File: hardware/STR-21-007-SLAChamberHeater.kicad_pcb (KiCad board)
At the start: 0 parts

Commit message: schematics finished, footprints assigned. Still need to fix foorptints for MOSFETS
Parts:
- added C101: 10n, Capacitor_SMD:C_0603_1608Metric, F.Cu at (88.9, 127.0)
- added C102: 10u, Capacitor_SMD:C_1206_3216Metric, F.Cu at (71.5, 132.3)
- added C103: 10u, Capacitor_SMD:C_1206_3216Metric, F.Cu at (90.3, 119.0)
- added C104: 10u, Capacitor_SMD:C_1206_3216Metric, F.Cu at (84.6, 122.3)
- added C201: 1u, Capacitor_SMD:C_0402_1005Metric, F.Cu at (75.3, 156.5)
- added C202: 10u, Capacitor_SMD:C_0402_1005Metric, F.Cu at (75.3, 158.5)
- added C203: 100n, Capacitor_SMD:C_0402_1005Metric, F.Cu at (79.7, 155.4)
- added C204: 100n, Capacitor_SMD:C_0402_1005Metric, F.Cu at (91.3, 143.4)
- added C301: 1u, Capacitor_SMD:C_0402_1005Metric, F.Cu at (136.1, 122.0)
- added C302: 100n, Capacitor_SMD:C_0402_1005Metric, F.Cu at (129.4, 127.6)
- added C303: 1u, Capacitor_SMD:C_0402_1005Metric, F.Cu at (132.3, 127.6)
- added C304: 100n, Capacitor_SMD:C_0402_1005Metric, F.Cu at (132.3, 125.6)
- added D101: B5819W, Diode_SMD:D_SOD-123, F.Cu at (92.2, 112.2)
- added D102: B5819W, Diode_SMD:D_SOD-123, F.Cu at (84.6, 119.0)
- added D103: B5819W, Diode_SMD:D_SOD-123, F.Cu at (65.8, 132.3)
- added D301: 1N4148W, Diode_SMD:D_SOD-123, F.Cu at (131.4, 112.2)
- added F101: 5A, Fuse:Fuse_1206_3216Metric, F.Cu at (92.1, 115.5)
- added FB101: 600@600MHz, Inductor_SMD:L_0805_2012Metric, F.Cu at (76.6, 132.0)
- added H1: MountingHole, MountingHole:MountingHole_2.2mm_M2, F.Cu at (113.5, 140.4)
- added H2: MountingHole, MountingHole:MountingHole_2.2mm_M2, F.Cu at (107.5, 146.3)
- added H3: MountingHole, MountingHole:MountingHole_2.2mm_M2, F.Cu at (107.5, 140.4)
- added H4: MountingHole, MountingHole:MountingHole_2.2mm_M2, F.Cu at (113.5, 146.3)
- added J101: 2.5mm, Connector_BarrelJack:BarrelJack_CUI_PJ-036AH-SMT_Horizontal, F.Cu at (72.3, 119.6)
- added J201: USB_C_Receptacle_USB2.0, STR-USB:USB_C_Receptacle_C136423, F.Cu at (44.5, 152.4)
- added J301: HEATER, TerminalBlock_Phoenix:TerminalBlock_Phoenix_PT-1,5-2-3.5-H_1x02_P3.50mm_Horizontal, F.Cu at (165.1, 127.0)
- added J302: FAN, Connector_JST:JST_EH_B2B-EH-A_1x02_P2.50mm_Vertical, F.Cu at (165.1, 139.7)
- added J401: OLED, Connector_PinHeader_2.54mm:PinHeader_1x04_P2.54mm_Vertical_SMD_Pin1Left, F.Cu at (134.4, 138.7)
- added L101: 10u, Inductor_SMD:L_Sunlord_MWSA0518_5.4x5.2mm, F.Cu at (85.5, 113.9)
- added LED101: Green, LED_SMD:LED_0603_1608Metric, F.Cu at (89.4, 121.9)
- added LED301: Blue, LED_SMD:LED_0603_1608Metric, F.Cu at (135.9, 117.8)
- added LED302: Red, LED_SMD:LED_0603_1608Metric, F.Cu at (135.9, 115.2)
- added LED401: WS2812B, STR-LED:WS2812B, F.Cu at (142.2, 154.1)
- added Q101: RU30L30M3, Package_DFN_QFN:DFN-8-1EP_3x3mm_P0.65mm_EP1.7x2.05mm, F.Cu at (152.4, 108.0)
- added Q301: BSS138, Package_TO_SOT_SMD:SOT-23, F.Cu at (129.3, 122.4)
- added Q302: RU30L30M3, Package_DFN_QFN:DFN-8-1EP_3x3mm_P0.65mm_EP1.7x2.05mm, F.Cu at (152.4, 120.7)
- added Q303: RU3070M3, STR-DFN:DFN-8-1EP_3x3mm_P0.65mm_EP1.7x2.05mm, F.Cu at (152.4, 114.3)
- added Q304: BSS138, Package_TO_SOT_SMD:SOT-23, F.Cu at (125.5, 127.0)
- added R101: 100K, Resistor_SMD:R_0603_1608Metric, F.Cu at (99.2, 116.3)
- added R102: 68K, Resistor_SMD:R_0603_1608Metric, F.Cu at (102.3, 111.8)
- added R103: 47K, Resistor_SMD:R_0603_1608Metric, F.Cu at (80.8, 131.8)
- added R104: 15K, Resistor_SMD:R_0603_1608Metric, F.Cu at (95.2, 118.4)
- added R105: 270, Resistor_SMD:R_0603_1608Metric, F.Cu at (93.5, 121.9)
- added R106: 1K5, Resistor_SMD:R_0603_1608Metric, F.Cu at (89.4, 124.5)
- added R201: 10K, Resistor_SMD:R_0402_1005Metric, F.Cu at (72.4, 156.5)
- added R202: 10K, Resistor_SMD:R_0402_1005Metric, F.Cu at (79.7, 153.4)
- added R203: 2k2, Resistor_SMD:R_0402_1005Metric, F.Cu at (69.5, 158.5)
- added R204: 2k2, Resistor_SMD:R_0402_1005Metric, F.Cu at (69.5, 156.5)
- added R205: 10K, Resistor_SMD:R_0402_1005Metric, F.Cu at (72.4, 158.5)
- added R207: 5K1, Resistor_SMD:R_0402_1005Metric, F.Cu at (82.6, 153.4)
- added R208: 5K1, Resistor_SMD:R_0402_1005Metric, F.Cu at (89.9, 148.4)
- added R301: 100R, Resistor_SMD:R_0402_1005Metric, F.Cu at (109.7, 128.1)
- added R302: 100R, Resistor_SMD:R_0402_1005Metric, F.Cu at (115.6, 128.1)
- added R303: 10K, Resistor_SMD:R_0402_1005Metric, F.Cu at (129.4, 125.6)
- added R304: 10K, Resistor_SMD:R_0402_1005Metric, F.Cu at (133.2, 120.1)
- added R305: 100R, Resistor_SMD:R_0402_1005Metric, F.Cu at (136.1, 120.1)
- added R306: 10K, Resistor_SMD:R_0402_1005Metric, F.Cu at (133.2, 122.1)
- added R307: 1K5, Resistor_SMD:R_0402_1005Metric, F.Cu at (112.7, 128.1)
- added R308: 1K5, Resistor_SMD:R_0402_1005Metric, F.Cu at (135.8, 111.5)
- added SW201: SW_Push, STR-Switch:SW_SMD_SPST_8x3.6, F.Cu at (101.6, 177.8)
- added SW202: SW_Push, STR-Switch:SW_SMD_SPST_8x3.6, F.Cu at (101.6, 165.1)
- added SW401: SW_Push, STR-Switch:SW_SMD_SPST_8x3.6, F.Cu at (127.0, 165.1)
- added SW402: SW_Push, STR-Switch:SW_SMD_SPST_8x3.6, F.Cu at (114.3, 165.1)
- added U101: MP2359DJ-LF-Z, Package_TO_SOT_SMD:SOT-23-6, F.Cu at (84.3, 126.2)
- added U201: ESP32-C3-MINI-1-N4, STR-ESP32:ESP32-C3-MINI-1-N4, F.Cu at (70.8, 146.5)
- added U202: USBLC6-2SC6, Package_TO_SOT_SMD:SOT-23-6, F.Cu at (65.5, 157.8)
- added U301: LM75BDP, Package_SO:MSOP-8-1EP_3x3mm_P0.65mm_EP1.68x1.88mm, F.Cu at (127.0, 152.4)
- added U302: MLX90614ESF-BAA-000-TU, STR-Sensors:TO254P942H425-4, F.Cu at (114.2, 115.9)
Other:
- copper layers 0 -> 2

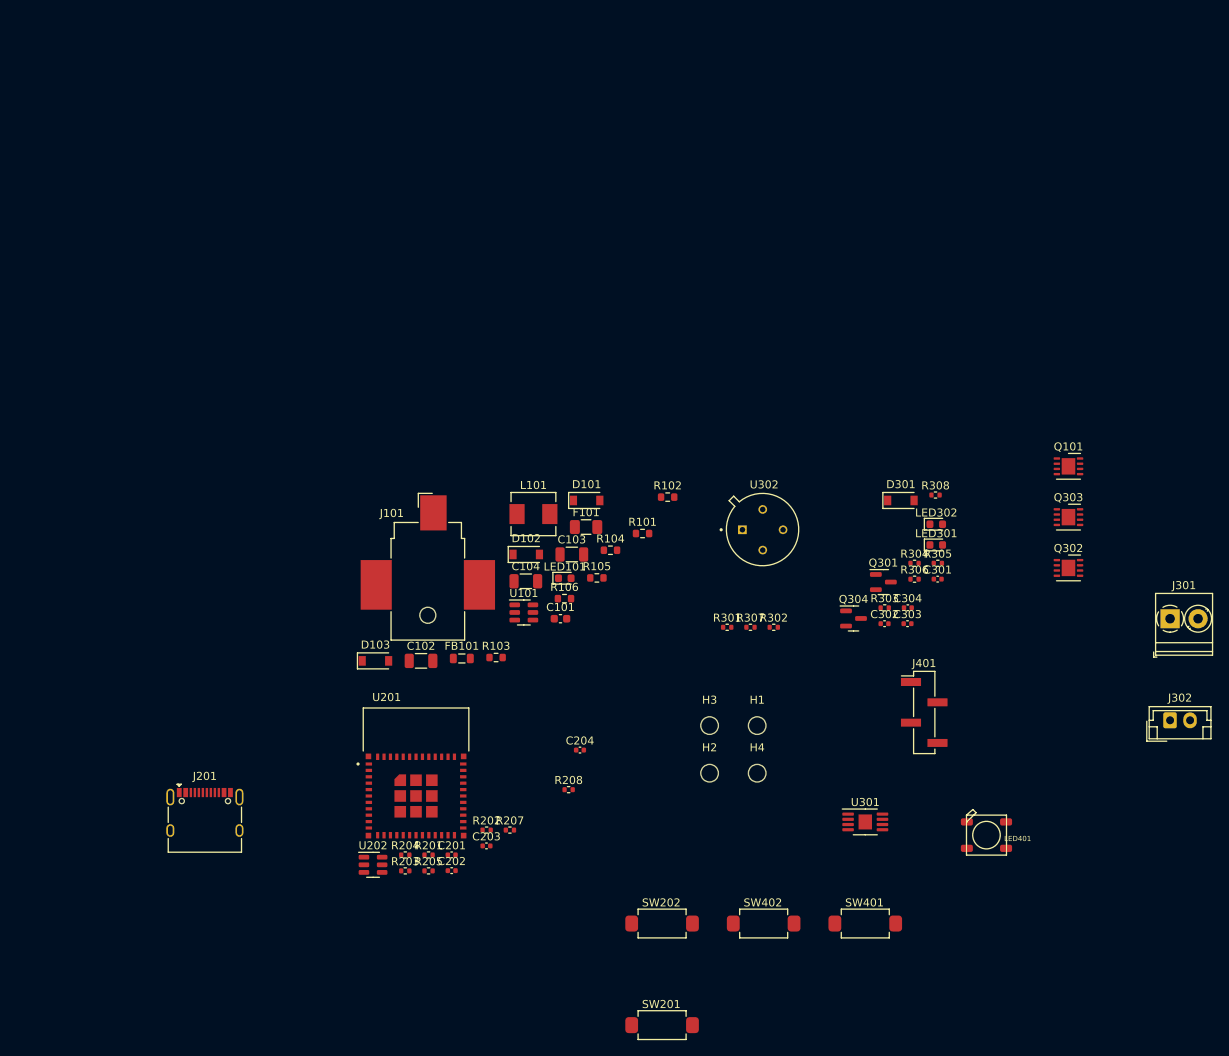
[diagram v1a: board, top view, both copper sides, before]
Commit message: footprint update for MOSFETS to PDFN3333
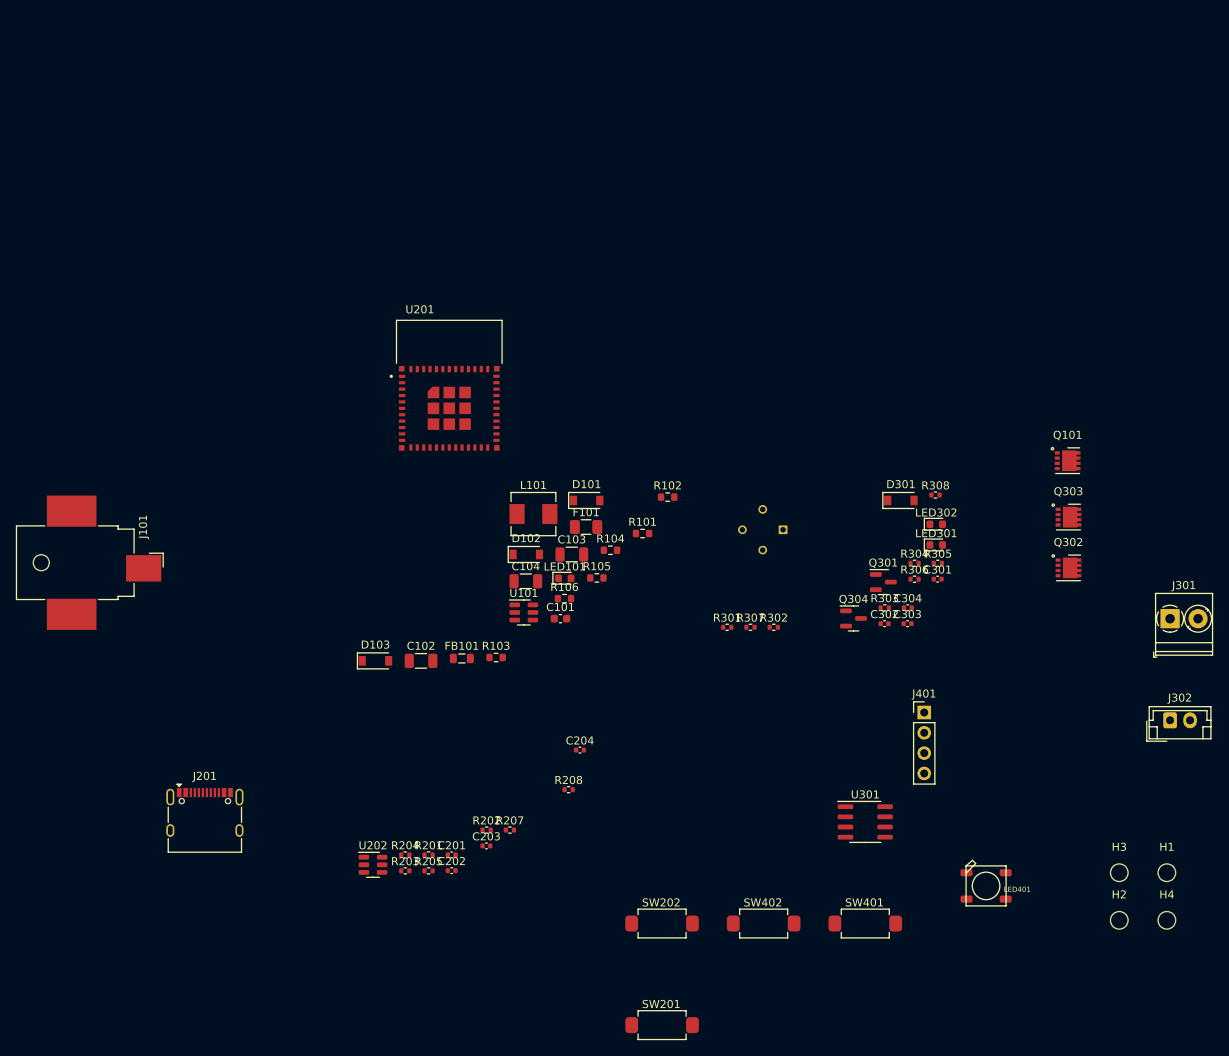
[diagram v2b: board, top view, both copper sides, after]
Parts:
- J401: footprint Connector_PinHeader_2.54mm:PinHeader_1x04_P2.54mm_Vertical_SMD_Pin1Left -> Connector_PinHeader_2.54mm:PinHeader_1x04_P2.54mm_Vertical
- Q101, Q302: footprint Package_DFN_QFN:DFN-8-1EP_3x3mm_P0.65mm_EP1.7x2.05mm -> STR-DFN:PDFN3333
- Q303: footprint STR-DFN:DFN-8-1EP_3x3mm_P0.65mm_EP1.7x2.05mm -> STR-DFN:PDFN3333
- U301: footprint Package_SO:MSOP-8-1EP_3x3mm_P0.65mm_EP1.68x1.88mm -> Package_SO:SOIC-8_3.9x4.9mm_P1.27mm
- U302: moved to B.Cu
- moved H1 54.4 mm to (164.7, 158.8)
- moved H2 54.4 mm to (158.8, 164.7)
- moved H3 54.4 mm to (158.8, 158.8)
- moved H4 54.4 mm to (164.7, 164.7)
- moved U201 48.6 mm to (75.0, 98.0)
- moved J101 41.3 mm to (31.0, 120.0), turned to -90 degrees
- moved LED401 6.35 mm to (142.1, 160.4)
- moved Q101 0.71 mm to (152.3, 107.2)
- turned U302 to 180 degrees
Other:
- copper layers 2 -> 4
- rule pad_to_mask_clearance: 0 -> 0.05

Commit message: routing and foot print changes
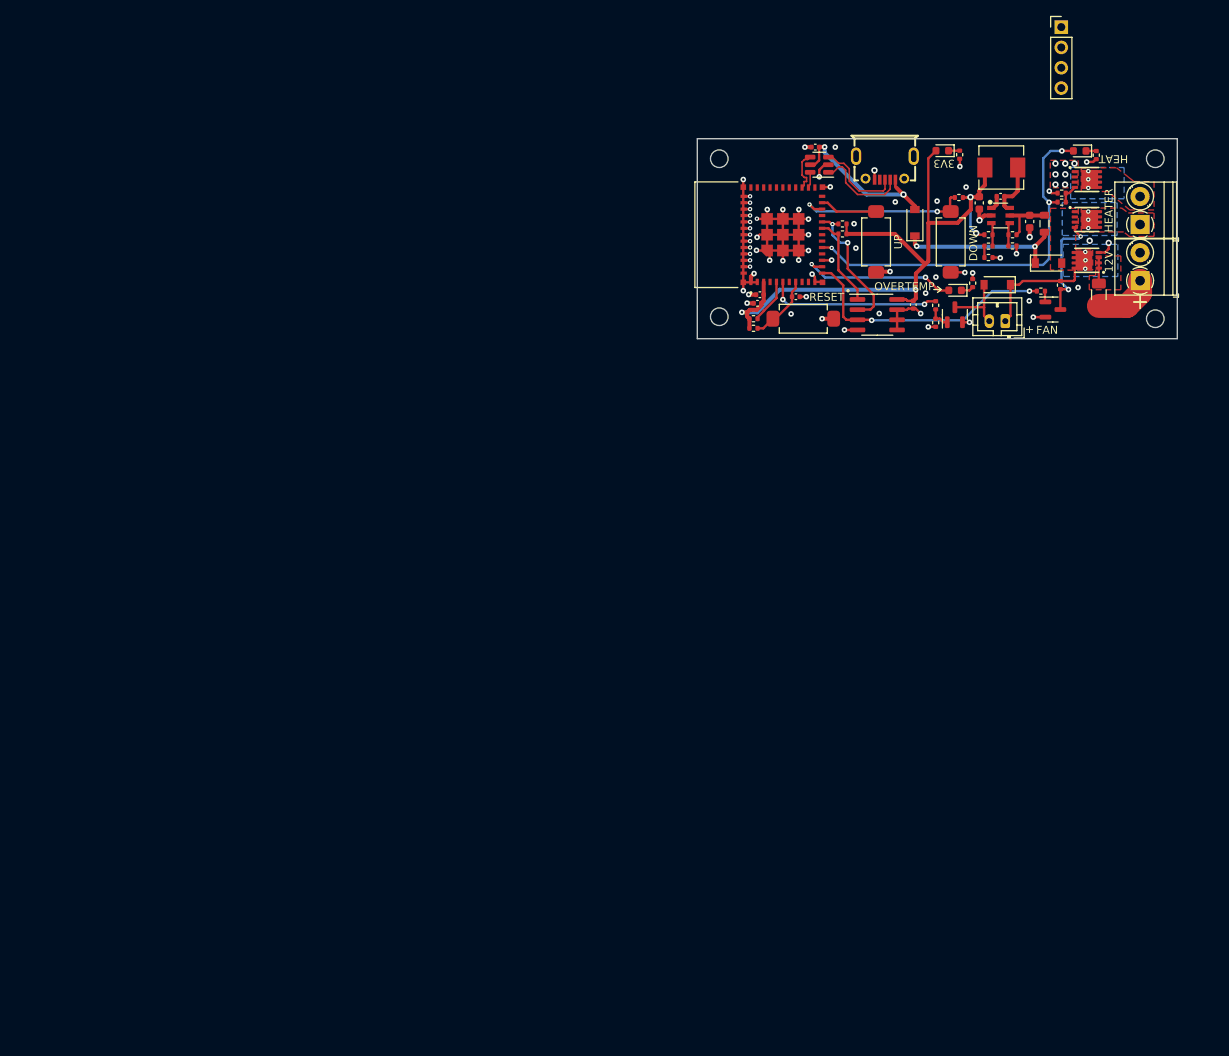
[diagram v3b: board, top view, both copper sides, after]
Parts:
- removed C104: 10u, Capacitor_SMD:C_1206_3216Metric
- removed C302, C304: 100n, Capacitor_SMD:C_0402_1005Metric
- removed C303: 1u, Capacitor_SMD:C_0402_1005Metric
- removed D103: B5819W, Diode_SMD:D_SOD-123
- removed J201: USB_C_Receptacle_USB2.0, STR-USB:USB_C_Receptacle_C136423
- removed LED401: WS2812B, STR-LED:WS2812B
- removed R207, R208: 5K1, Resistor_SMD:R_0402_1005Metric
- removed SW402: SW_Push, STR-Switch:SW_SMD_SPST_8x3.6
- removed U302: MLX90614ESF-BAA-000-TU, STR-Sensors:TO254P942H425-4
- added USB201: U-F-M5DD-Y-L, STR-USB:MICRO-USB-SMD_MICRO-USB-18, F.Cu at (129.5, 70.7)
- C101: footprint Capacitor_SMD:C_0603_1608Metric -> Capacitor_SMD:C_0402_1005Metric
- C102: footprint Capacitor_SMD:C_1206_3216Metric -> Capacitor_SMD:C_0603_1608Metric
- C103: value 10u -> 22u; footprint Capacitor_SMD:C_1206_3216Metric -> Capacitor_SMD:C_0603_1608Metric
- C301: value 1u -> 100n
- J101: footprint Connector_BarrelJack:BarrelJack_CUI_PJ-036AH-SMT_Horizontal -> TerminalBlock_Phoenix:TerminalBlock_Phoenix_PT-1,5-2-3.5-H_1x02_P3.50mm_Horizontal
- J302: footprint Connector_JST:JST_EH_B2B-EH-A_1x02_P2.50mm_Vertical -> Connector_JST:JST_PH_B2B-PH-K_1x02_P2.00mm_Vertical
- Q101, Q302, Q303: footprint STR-DFN:PDFN3333 -> STR-DFN:DFN-8_L3.0-W3.0-P0.65-BL
- R101, R102, R103, R104, R105, R106: footprint Resistor_SMD:R_0603_1608Metric -> Resistor_SMD:R_0402_1005Metric
- U101: footprint Package_TO_SOT_SMD:SOT-23-6 -> STR-DFN:SOT-23-6_L2.9-W1.6-P0.95-LS2.8-BL
- moved J101 135.0 mm to (161.4, 84.8), turned to 90 degrees
- moved R205 107.1 mm to (138.7, 74.3), turned to 180 degrees
- moved U202 103.8 mm to (121.2, 70.2), turned to 180 degrees
- moved H3 102.3 mm to (108.8, 69.5)
- moved R203 96.6 mm to (124.2, 78.9), turned to 180 degrees
- moved R204 96.0 mm to (124.2, 77.7), turned to 180 degrees
- moved H4 95.2 mm to (163.2, 69.5)
- moved C102 93.8 mm to (147.6, 77.3), turned to -90 degrees
- moved FB101 90.9 mm to (149.4, 77.6), turned to 90 degrees
- moved H2 90.5 mm to (108.8, 89.2)
- moved SW201 90.0 mm to (119.2, 89.5), turned to 180 degrees
- moved SW202 89.3 mm to (128.3, 79.9), turned to 90 degrees
- moved J401 87.4 mm to (151.5, 53.0)
- moved SW401 85.9 mm to (137.7, 79.9), turned to 90 degrees
- moved C202 82.0 mm to (118.3, 86.8)
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- renumbered C202 to C201, C201 to C202, R202 to R201, R201 to R202, R307 to R306, R306 to R307
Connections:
- net Net-(F101-Pad2) renamed /[1] Power/FUSE_S
- R201 pad 2: NEOPIX -> unconnected-(R201-Pad2)
- U201 pad 12: HEATER -> ~{INT_OVERTEMP}
- U201 pad 13: ~{INT_OVERTEMP} -> OVERTEMP
- U201 pad 16: unconnected-(U201-Pad16) -> HEATER
- U201 pad 18: FAN -> unconnected-(U201-Pad18)
- U201 pad 21: OVERTEMP -> unconnected-(U201-Pad21)
- U201 pad 5: NEOPIX -> unconnected-(R201-Pad2)
- U201 pad 6: BTN2 -> FAN
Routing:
- net GND: track 0.00 -> 104.8 mm, vias 0 -> 73
- net +3V3: track 0.00 -> 86.1 mm, vias 0 -> 4
- net HEATER: track 0.00 -> 47.7 mm, vias 0 -> 3
- net ~{INT_OVERTEMP}: track 0.00 -> 33.1 mm, vias 0 -> 2
- net BTN1: track 0.00 -> 22.1 mm, vias 0 -> 2
- net FAN: track 0.00 -> 21.7 mm, vias 0 -> 2
- net VBUS: track 0.00 -> 21.2 mm, vias 0 -> 2
- net Net-(D101-Pad1): track 0.00 -> 20.6 mm, vias 0 -> 2
- net OVERTEMP: track 0.00 -> 20.0 mm, vias 0 -> 2
- net I2C1_SCL: track 0.00 -> 17.4 mm, vias 0 -> 2
- net 12V_FUSED: track 0.00 -> 14.6 mm, vias 0 -> 3
- net /[3] Heater/OT_G: track 0.00 -> 14.1 mm, vias 0 -> 2
- net /[2] MCU/USB_CONN_D-: track 0.00 -> 11.8 mm
- net I2C1_SDA: track 0.00 -> 11.5 mm
- net /[2] MCU/USB_CONN_D+: track 0.00 -> 11.0 mm
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- added copper zone on F.Cu, net /[1] Power/FUSE_S
- added copper zone on B.Cu, net /[3] Heater/HEAT_CONN_1
- added copper zone on F.Cu, net /[3] Heater/HEAT_CONN_1
- added copper zone on B.Cu, net /[3] Heater/HEAT_CONN_2
- added copper zone on F.Cu, net /[3] Heater/HEAT_CONN_2
- added copper zone on B.Cu, net 12V_FUSED
- added copper zone on F.Cu, net 12V_FUSED
- added copper zone on F.Cu, net GND
- added copper zone on In1.Cu, net GND
- added copper zone on In2.Cu, net GND
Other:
- board outline added: 60 x 25 mm
- board text added: "+"
- board text added: "12V"
- board text added: "3V3"
- board text added: "DOWN"
- board text added: "FAN"
- board text added: "HEAT"
- board text added: "HEATER"
- board text added: "OVERTEMP"
- board text added: "RESET"
- board text added: "UP"

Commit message: DRC
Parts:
- removed J401: OLED, Connector_PinHeader_2.54mm:PinHeader_1x04_P2.54mm_Vertical
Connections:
- USB201 pad 0: unconnected-(USB201-Pad0) -> (no net)
